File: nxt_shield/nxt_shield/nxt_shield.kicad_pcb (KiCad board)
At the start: 2 copper layers, 99 x 54 mm, 87 parts, among them J1 NXT_M0, J10 NXT_SENS0, J11 NXT_SENS0, J12 NXT_SENS0, J13 NXT_SENS0, J14 NXT_SENS0, J15 NXT_SENS0, J16 NXT_SENS0, J17 RB_I2C1, J18 RB_I2C0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

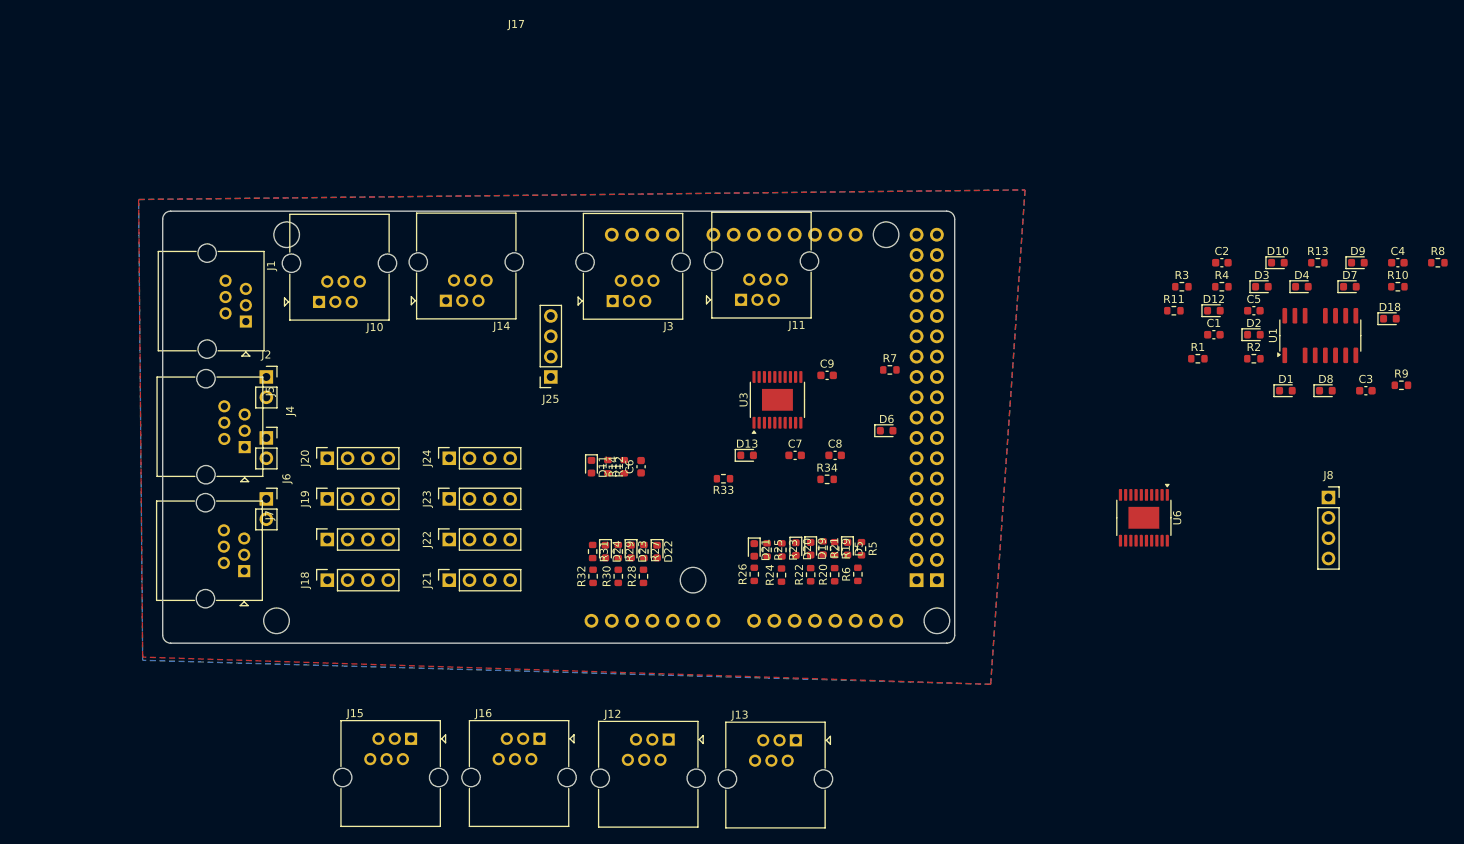
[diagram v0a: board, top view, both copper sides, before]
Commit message: first version of NXT shield with nxt sensors
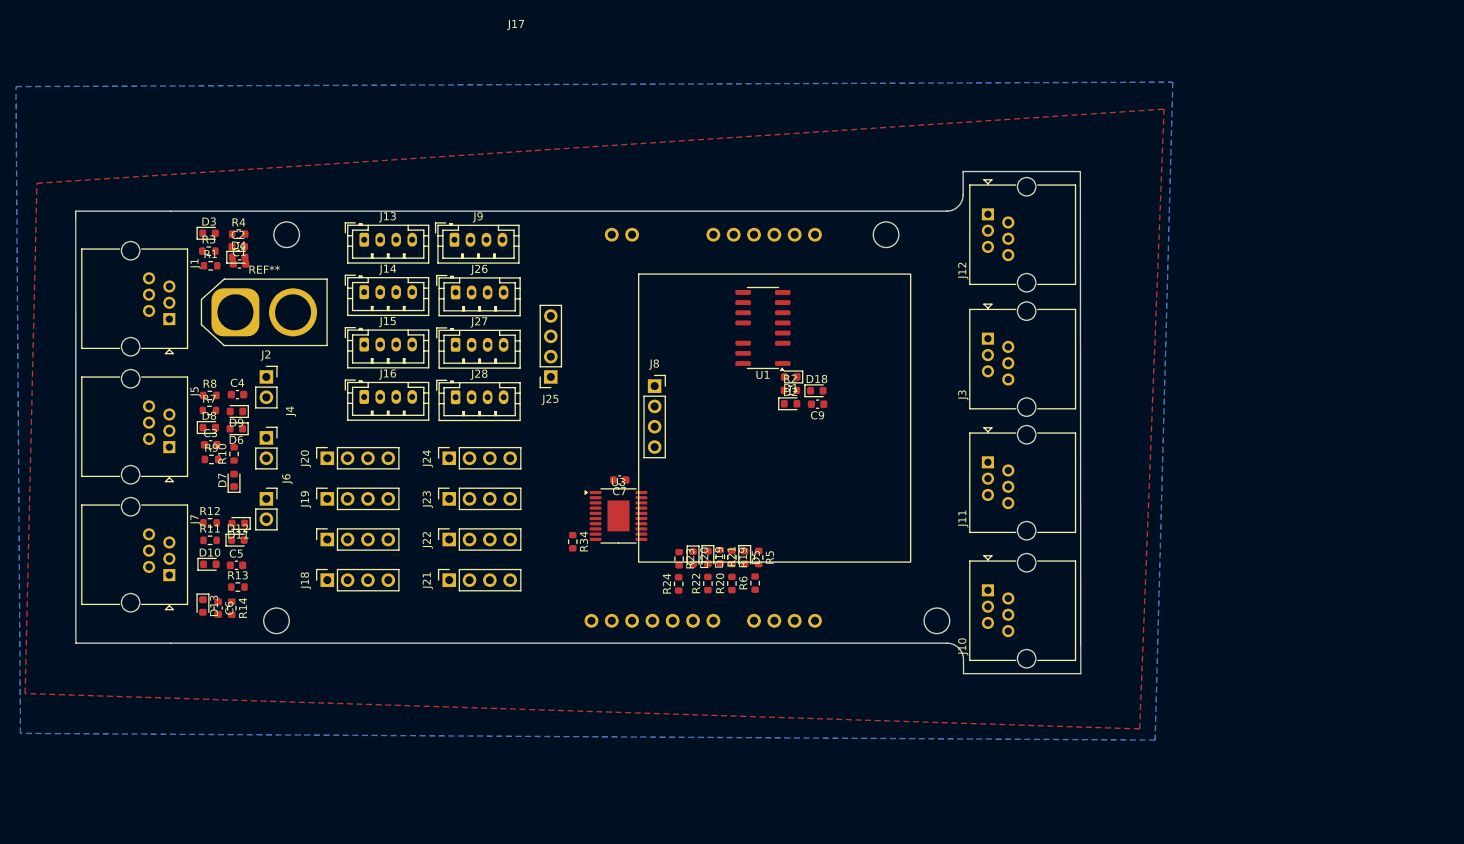
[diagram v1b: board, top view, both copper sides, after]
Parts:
- removed C8: 100n, Capacitor_SMD:C_0603_1608Metric
- removed D21, D22, D23, D24: D, Diode_SMD:D_0603_1608Metric
- removed R25, R26, R27, R28, R29, R30, R31, R32: 1k, Resistor_SMD:R_0603_1608Metric
- removed R33: 820, Resistor_SMD:R_0603_1608Metric
- removed U6: TPS4H000, Package_SO:HTSSOP-20-1EP_4.4x6.5mm_P0.65mm_EP2.74x3.86mm
- added J26: JST_RB_I2C5, Connector_JST:JST_PH_B4B-PH-K_1x04_P2.00mm_Vertical, F.Cu at (128.6, 65.6)
- added J27: JST_RB_I2C6, Connector_JST:JST_PH_B4B-PH-K_1x04_P2.00mm_Vertical, F.Cu at (128.6, 72.2)
- added J28: JST_RB_I2C7, Connector_JST:JST_PH_B4B-PH-K_1x04_P2.00mm_Vertical, F.Cu at (128.6, 78.7)
- added J9: JST_RB_I2C0, Connector_JST:JST_PH_B4B-PH-K_1x04_P2.00mm_Vertical, F.Cu at (128.4, 59.1)
- added REF**: AMASS_XT60-M_1x02_P7.20mm_Vertical, Connector_AMASS:AMASS_XT60-M_1x02_P7.20mm_Vertical, F.Cu at (101.0, 68.1)
- J13: value NXT_SENS0 -> JST_RB_I2C1; footprint Connector_RJ:RJ25_Wayconn_MJEA-660X1_Horizontal -> Connector_JST:JST_PH_B4B-PH-K_1x04_P2.00mm_Vertical
- J14: value NXT_SENS0 -> JST_RB_I2C2; footprint Connector_RJ:RJ25_Wayconn_MJEA-660X1_Horizontal -> Connector_JST:JST_PH_B4B-PH-K_1x04_P2.00mm_Vertical
- J15: value NXT_SENS0 -> JST_RB_I2C3; footprint Connector_RJ:RJ25_Wayconn_MJEA-660X1_Horizontal -> Connector_JST:JST_PH_B4B-PH-K_1x04_P2.00mm_Vertical
- J16: value NXT_SENS0 -> JST_RB_I2C4; footprint Connector_RJ:RJ25_Wayconn_MJEA-660X1_Horizontal -> Connector_JST:JST_PH_B4B-PH-K_1x04_P2.00mm_Vertical
- moved R8 154.4 mm to (97.8, 78.5)
- moved R9 149.0 mm to (98.0, 86.5)
- moved R10 147.0 mm to (100.9, 85.8), turned to 90 degrees
- moved C4 146.0 mm to (101.3, 78.4)
- moved C3 144.6 mm to (97.9, 84.7)
- moved D7 141.6 mm to (100.9, 89.1), turned to 90 degrees
- moved D9 141.4 mm to (101.2, 80.5), turned to 180 degrees
- moved R13 141.0 mm to (101.3, 102.5)
- moved D8 139.7 mm to (97.8, 82.5)
- moved D10 138.7 mm to (97.8, 99.6)
- moved D4 132.9 mm to (101.4, 61.2)
- moved D3 131.8 mm to (97.7, 58.2)
- moved C5 131.1 mm to (101.2, 99.7)
- moved D12 125.3 mm to (101.3, 96.6)
- moved R1 123.9 mm to (97.9, 62.3)
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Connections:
- A1 pad A1: SENS7_ADC -> SENS_P4
- A1 pad A10: unconnected-(A1-PadA10) -> SENS_DIAG0
- A1 pad A11: unconnected-(A1-PadA11) -> THERMAL_0
- A1 pad A2: SENS6_ADC -> SENS_P3
- A1 pad A3: SENS5_ADC -> SENS_P2
- A1 pad A4: SENS4_ADC -> SENS_P1
- A1 pad A9: unconnected-(A1-PadA9) -> SENS_DIAG1
- A1 pad D14: unconnected-(A1-D14/TX3-PadD14) -> ENC_M2_DIR
- A1 pad D15: unconnected-(A1-D15/RX3-PadD15) -> ENC_M1_DIR
- A1 pad D16: unconnected-(A1-D16/TX2-PadD16) -> ENC_M0_DIR
- A1 pad D17: unconnected-(A1-D17/RX2-PadD17) -> ENC_M2_INT
- A1 pad D18: unconnected-(A1-D18/TX1-PadD18) -> ENC_M1_INT
- A1 pad D19: unconnected-(A1-D19/RX1-PadD19) -> ENC_M0_INT
- A1 pad D2: unconnected-(A1-PadD2) -> SENS_DIAG3
- A1 pad D3: unconnected-(A1-PadD3) -> SENS_DIAG2
- J13 pad 1: SENS4_9V -> SDA1
- J13 pad 3: GND -> SCL1
- J13 pad 4: +5V -> +3.3V
- J14 pad 1: SENS5_9V -> SDA2
- J14 pad 3: GND -> SCL2
- J14 pad 4: +5V -> +3.3V
- J15 pad 1: SENS6_9V -> SDA3
- J15 pad 3: GND -> SCL3
- J15 pad 4: +5V -> +3.3V
- J16 pad 1: SENS7_9V -> SDA4
- J16 pad 3: GND -> SCL4
- J16 pad 4: +5V -> +3.3V
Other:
- board size 99 x 54 mm -> 125.6 x 62.8 mm

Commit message: nxt shield first prototype production
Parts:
- removed C7: 100n, Capacitor_SMD:C_0603_1608Metric
- removed D18, D19, D20, D5: D, Diode_SMD:D_0603_1608Metric
- removed J11, J12: NXT_SENS0, Connector_RJ:RJ25_Wayconn_MJEA-660X1_Horizontal
- removed R19, R20, R21, R22, R23, R24, R5, R6: 1k, Resistor_SMD:R_0603_1608Metric
- removed R34: 820, Resistor_SMD:R_0603_1608Metric
- removed REF**: AMASS_XT60-M_1x02_P7.20mm_Vertical, Connector_AMASS:AMASS_XT60-M_1x02_P7.20mm_Vertical
- removed U3: TPS4H000, Package_SO:HTSSOP-20-1EP_4.4x6.5mm_P0.65mm_EP2.74x3.86mm
- added G***: LOGO, external_libs:RocciLogo, F.Cu at (116.6, 106.2)
- added G***: LOGO, external_libs:RocciLogo, B.Cu at (132.3, 106.7)
- added ON/OFF: SW_SPDT, CustomFootprints:XKB Connection SS-12M11G5, F.Cu at (115.1, 76.4)
- added SW1_A9: SW_Push, Button_Switch_THT:SW_PUSH_6mm, F.Cu at (158.6, 101.9)
- added SW2_A10: SW_Push, Button_Switch_THT:SW_PUSH_6mm, F.Cu at (168.7, 101.9)
- added SW3_A11: SW_Push, Button_Switch_THT:SW_PUSH_6mm, F.Cu at (178.9, 101.9)
- C1, C2, C3, C4, C5, C6: footprint Capacitor_SMD:C_0603_1608Metric -> Capacitor_SMD:C_0805_2012Metric_Pad1.18x1.45mm_HandSolder
- C9 100n: renamed from C9; footprint Capacitor_SMD:C_0603_1608Metric -> Capacitor_SMD:C_0805_2012Metric_Pad1.18x1.45mm_HandSolder
- D1, D10, D11, D12, D13, D2, D3, D4, D6, D7, D8, D9: footprint Diode_SMD:D_0603_1608Metric -> Diode_SMD:D_0805_2012Metric_Pad1.15x1.40mm_HandSolder
- J17, J18, J19, J20, J21, J22, J23, J24, J25: moved to B.Cu
- J3: value NXT_SENS0 -> XT60_PCB; footprint Connector_RJ:RJ25_Wayconn_MJEA-660X1_Horizontal -> Connector_AMASS:AMASS_XT60-M_1x02_P7.20mm_Vertical; moved to B.Cu
- J4: value RB_M0 -> RB_M2; moved to B.Cu
- J6: value RB_M0 -> RB_M1; moved to B.Cu
- J8: footprint Connector_PinSocket_2.54mm:PinSocket_1x04_P2.54mm_Vertical -> CustomFootprints:OLE_LCD
- R1, R10, R11, R12, R13, R14, R2, R3, R4, R7, R8, R9: footprint Resistor_SMD:R_0603_1608Metric -> Resistor_SMD:R_0805_2012Metric_Pad1.20x1.40mm_HandSolder
- RB 7V: renamed from J2; value RB_M0 -> RB_M3; moved to B.Cu
- U1 74HC14: renamed from U1; footprint Package_SO:SOIC-14-16_3.9x9.9mm_P1.27mm -> Package_SO:SO-14_3.9x8.65mm_P1.27mm
- VIN_7V: renamed from J10; value NXT_SENS0 -> XT60_Case; footprint Connector_RJ:RJ25_Wayconn_MJEA-660X1_Horizontal -> Connector_AMASS:AMASS_XT60IPW-M_1x03_P7.20mm_Horizontal
- moved J3 94.1 mm to (101.0, 68.1), turned to 0 degrees
- moved D13 86.3 mm to (175.5, 69.1), turned to 0 degrees
- moved D8 78.3 mm to (175.5, 73.2)
- moved D12 77.2 mm to (175.5, 75.3)
- moved VIN_7V 77.0 mm to (124.5, 72.2), turned to 0 degrees
- moved D10 76.1 mm to (169.9, 75.3)
- moved D9 74.9 mm to (175.5, 71.2), turned to 0 degrees
- moved D4 74.2 mm to (175.5, 65.0)
- moved D11 73.1 mm to (169.9, 69.1), turned to 0 degrees
- moved R14 72.5 mm to (169.9, 83.8), turned to 0 degrees
- moved D3 72.5 mm to (169.9, 65.0)
- moved R9 71.9 mm to (169.9, 87.9)
- moved R4 71.7 mm to (169.9, 79.8)
- moved D7 71.4 mm to (169.9, 71.2), turned to 0 degrees
- moved R12 71.1 mm to (164.3, 69.1)
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- renumbered J7 to M1, J5 to M2, J1 to M3
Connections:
- net Net-(J1-Pin_1) renamed /M0A
- net Net-(J1-Pin_2) renamed /M0B
- net Net-(J4-Pin_1) renamed /M1A
- net Net-(J4-Pin_2) renamed /M1B
- net Net-(J6-Pin_1) renamed /M2A
- net Net-(J6-Pin_2) renamed /M2B
- A1 pad A1: SENS_P4 -> (no net)
- A1 pad A10: SENS_DIAG0 -> Button2
- A1 pad A11: THERMAL_0 -> Button3
- A1 pad A2: SENS_P3 -> (no net)
- A1 pad A3: SENS_P2 -> (no net)
- A1 pad A4: SENS_P1 -> (no net)
- A1 pad A5: SENS3_ADC -> unconnected-(A1-PadA5)
- A1 pad A6: SENS2_ADC -> unconnected-(A1-PadA6)
- A1 pad A7: SENS1_ADC -> unconnected-(A1-PadA7)
- A1 pad A8: SENS0_ADC -> unconnected-(A1-PadA8)
- A1 pad A9: SENS_DIAG1 -> Button1
- J13 pad 4: +3.3V -> VDDI2C1
- J14 pad 4: +3.3V -> VDDI2C2
- J15 pad 4: +3.3V -> VDDI2C3
- J16 pad 4: +3.3V -> VDDI2C4
- J17 pad 4: +3.3V -> VDDI2C1
- J18 pad 4: +3.3V -> VDDI2C0
- J19 pad 4: +3.3V -> VDDI2C2
- J20 pad 4: +3.3V -> VDDI2C3
- J21 pad 4: +3.3V -> VDDI2C4
- J22 pad 4: +3.3V -> VDDI2C5
- J23 pad 4: +3.3V -> VDDI2C6
- J24 pad 4: +3.3V -> VDDI2C7
- J26 pad 4: +3.3V -> VDDI2C5
- J27 pad 4: +3.3V -> VDDI2C6
- J28 pad 4: +3.3V -> VDDI2C7
- J3 pad 1: SENS0_9V -> GND
- J3 pad 2: GND -> /AKKU1
- J8 pad 3: GND -> +5V
- J8 pad 4: +5V -> GND
- J9 pad 4: +3.3V -> VDDI2C0
- VIN_7V pad 1: SENS1_9V -> GND
- VIN_7V pad 2: GND -> /AKKU2
- VIN_7V pad 3: GND -> (no net)
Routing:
- net ENC_M2_A: track 0.00 -> 123.5 mm, vias 0 -> 1
- net ENC_M2_B: track 0.00 -> 116.7 mm, vias 0 -> 1
- net +5V: track 0.00 -> 106.5 mm
- net ENC_M1_A: track 0.00 -> 101.8 mm, vias 0 -> 1
- net ENC_M1_B: track 0.00 -> 100.2 mm, vias 0 -> 1
- net ENC_M0_B: track 0.00 -> 74.1 mm, vias 0 -> 1
- net ENC_M0_A: track 0.00 -> 72.6 mm, vias 0 -> 1
- net +3.3V: track 0.00 -> 66.5 mm, vias 0 -> 2
- net Net-(D3-A): track 0.00 -> 63.8 mm, vias 0 -> 4
- net Net-(D1-A): track 0.00 -> 57.4 mm, vias 0 -> 4
- net Net-(D6-A): track 0.00 -> 57.0 mm, vias 0 -> 4
- net Net-(D11-A): track 0.00 -> 50.7 mm, vias 0 -> 4
- net Net-(D7-A): track 0.00 -> 48.5 mm, vias 0 -> 4
- net SDA3: track 0.00 -> 46.9 mm
- net VDDI2C3: track 0.00 -> 45.5 mm
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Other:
- board size 125.6 x 62.8 mm -> 107 x 54 mm
- board text added: "C 100p"
- board text added: "D"
- board text added: "D14"
- board text added: "D15"
- board text added: "D16"
- board text added: "D17"
- board text added: "D18"
- board text added: "D19"
- board text added: "NXT-Shield V0.1 2.11.2025"
- board text added: "R 10k"
- board text added: "R_1M"
- board text added: "SDA GND SCL VDD"
